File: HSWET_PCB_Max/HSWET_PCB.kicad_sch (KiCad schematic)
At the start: 21 parts, among them IC3 PS2565L-1-V-F3-A, IC4 PS2565L-1-V-F3-A, IC5 PS2565L-1-V-F3-A, J1 CON-SOCJ-2155, J2 emergency stop, J3 CON-SOCJ-2155, J4 turbine bus, U1 INA260AIPWR, U3 YAAJ_DCDC_StepDown_LM2596

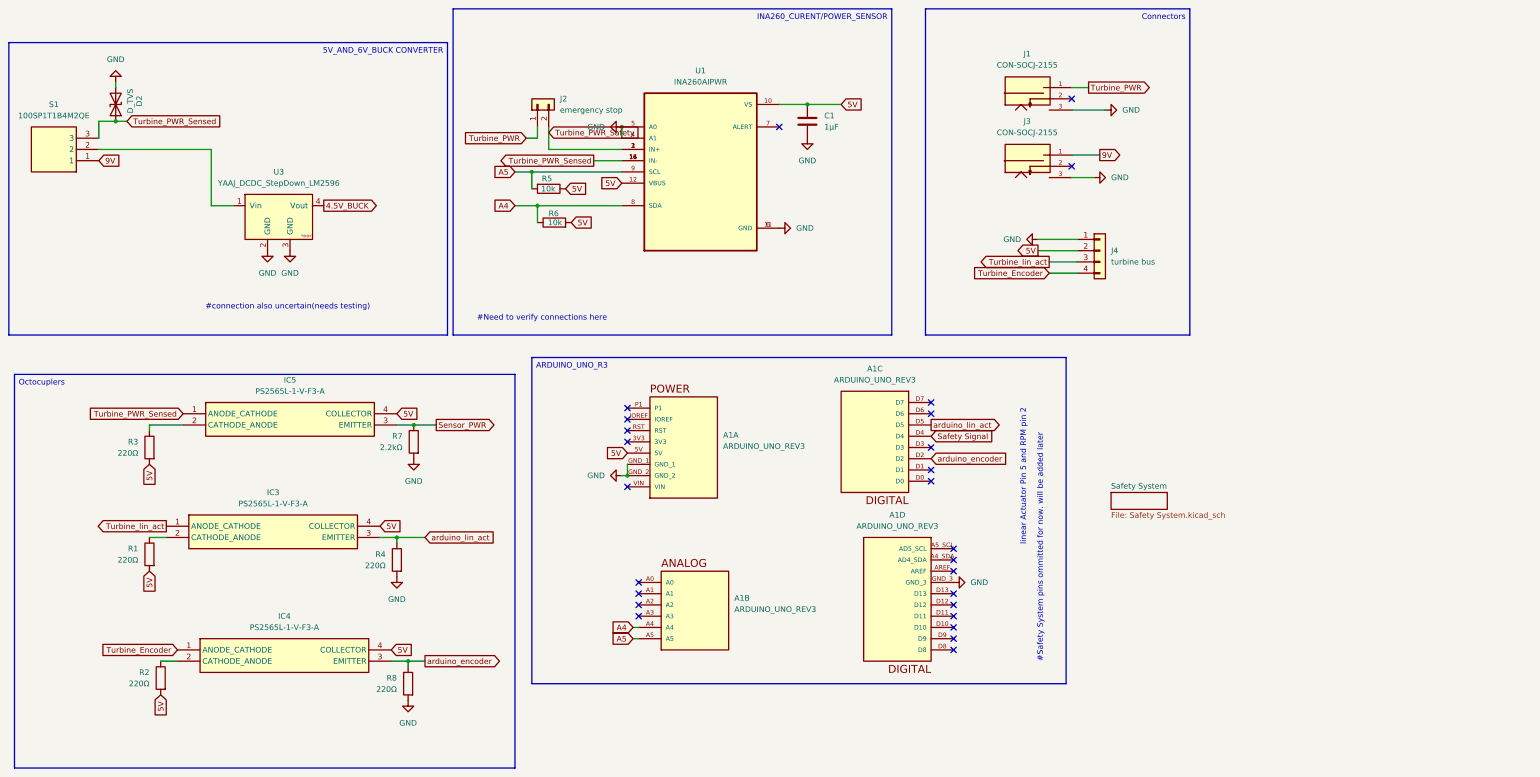
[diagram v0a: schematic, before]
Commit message: labelled everything, cleanup up various things, corrected inductor, removed schmitt
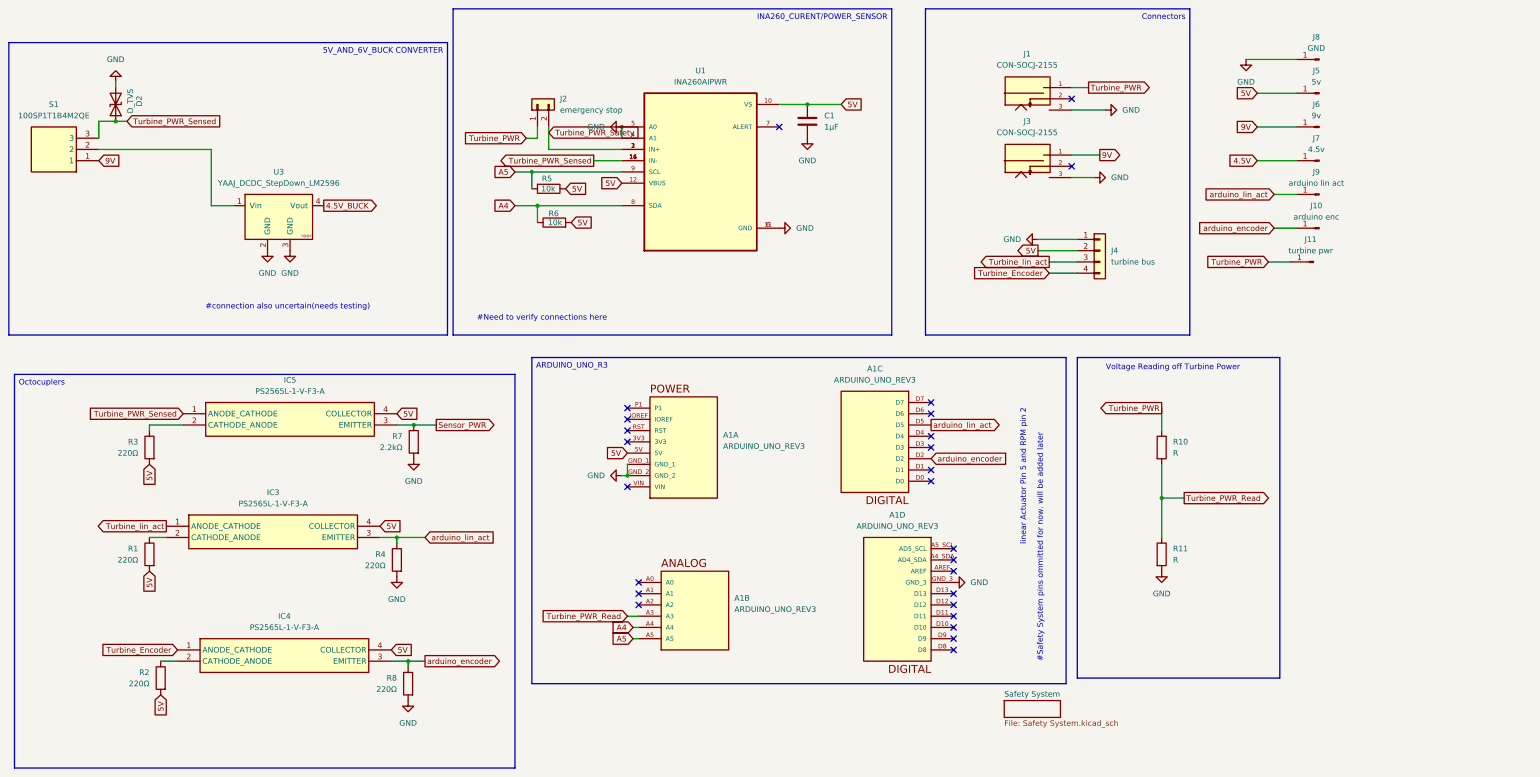
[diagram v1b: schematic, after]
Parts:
- added J10: arduino enc, Connector_PinHeader_1.00mm:PinHeader_1x01_P1.00mm_Vertical, symbol Connector:Conn_01x01_Pin
- added J11: turbine pwr, Connector_PinHeader_1.00mm:PinHeader_1x01_P1.00mm_Vertical, symbol Connector:Conn_01x01_Pin
- added J5: 5v, Connector_PinHeader_1.00mm:PinHeader_1x01_P1.00mm_Vertical, symbol Connector:Conn_01x01_Pin
- added J6: 9v, Connector_PinHeader_1.00mm:PinHeader_1x01_P1.00mm_Vertical, symbol Connector:Conn_01x01_Pin
- added J7: 4.5v, Connector_PinHeader_1.00mm:PinHeader_1x01_P1.00mm_Vertical, symbol Connector:Conn_01x01_Pin
- added J8: GND, Connector_PinHeader_1.00mm:PinHeader_1x01_P1.00mm_Vertical, symbol Connector:Conn_01x01_Pin
- added J9: arduino lin act, Connector_PinHeader_1.00mm:PinHeader_1x01_P1.00mm_Vertical, symbol Connector:Conn_01x01_Pin
- added R10, R11: R, Resistor_THT:R_Axial_DIN0207_L6.3mm_D2.5mm_P10.16mm_Horizontal, symbol Device:R
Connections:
- net 5V: now also J5.1 (Pin_1)
- net 9V: now also J6.1 (Pin_1)
- net GND: now also J8.1 (Pin_1), R11.2
- net Turbine_PWR: now also J11.1 (Pin_1), R10.1
- net arduino_encoder: now also J10.1 (Pin_1)
- net arduino_lin_act: now also J9.1 (Pin_1)
- net Turbine_PWR_Read: now reaches A1.A3
- net Turbine_PWR_Read: now also R10.2, R11.1
- net Safety Signal: no longer names the net of A1.D4
- new net 4.5V: J7.1 (Pin_1)
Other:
- note added: "Voltage Reading off Turbine Power"

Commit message: bruh
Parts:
- removed J1: CON-SOCJ-2155, footprints:GRAVITECH_CON-SOCJ-2155, symbol CON-SOCJ-2155:CON-SOCJ-2155
- added J1: TURBINE_IN, Connector_AMASS:AMASS_XT30PW-M_1x02_P2.50mm_Horizontal, symbol Connector_Generic:Conn_01x02
- added J12: LOAD_OUT, Connector_AMASS:AMASS_XT30PW-M_1x02_P2.50mm_Horizontal, symbol Connector_Generic:Conn_01x02
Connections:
- net GND: now also J1.2 (Pin_2), J12.2 (Pin_2)
- net Sensor_PWR: now also A1.A2
- net Turbine_PWR: now also J1.1 (Pin_1)
- net Turbine_PWR_Sensed: now also J12.1 (Pin_1)
- no-connect marks 26 -> 24

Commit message: made traces for power muuuuuuuuuuuuch bigger and added connector for load and removed 9v stuff just plug into the turbine
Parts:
- removed J3: CON-SOCJ-2155, footprints:GRAVITECH_CON-SOCJ-2155, symbol CON-SOCJ-2155:CON-SOCJ-2155
- removed J6: 9v, Connector_PinHeader_1.00mm:PinHeader_1x01_P1.00mm_Vertical, symbol Connector:Conn_01x01_Pin
- removed S1: 100SP1T1B4M2QE, footprints:100SP1T1B4M2QE, symbol 100SP1T1B4M2QE:100SP1T1B4M2QE
- J2: footprint Connector_PinHeader_2.54mm:PinHeader_1x02_P2.54mm_Vertical -> Connector_JST:JST_EH_B2B-EH-A_1x02_P2.50mm_Vertical
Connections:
- net 4.5V is gone; now on net 4.5V_BUCK: J7.1 (Pin_1)
- net Turbine_PWR_Sensed: now also U3.1 (Vin)
- no-connect marks 24 -> 23
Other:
- note added: "diode drains anything 40V+ to protect circuit :DDDDDDDDD"

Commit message: fixed lin act schematci
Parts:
- A1, IC3, IC4, IC5, J1, J12, J2, J4, U3: now not fitted
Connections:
- net 5V: no longer R1.2
- net GND: now also R1.2
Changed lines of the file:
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@@
 	(wire
 		(pts
-			(xy 137.16 40.64) (xy 137.16 45.72)
-		)
-		(stroke
-			(width 0)
-			(type default)
-		)
-	)
-	(wire
-		(pts
 			(xy 275.59 116.84) (xy 275.59 124.46)
 		)
@@
 	(wire
 		(pts
+			(xy 137.16 40.64) (xy 137.16 45.72)
+		)
+		(stroke
+			(width 0)
+			(type default)
+		)
+	)
+	(wire
+		(pts
 			(xy 134.62 43.18) (xy 134.62 40.64)
 		)
@@
 	)
 	(global_label "5V"
-		(shape input)
-		(at 46.99 140.97 270)
-		(fields_autoplaced yes)
-		(effects
-			(font
-				(size 1.27 1.27)
-			)
-			(justify right)
-		)
-		(property "Intersheetrefs" "${INTERSHEET_REFS}"
-			(at 46.99 146.2533 90)
-			(effects
-				(font
-					(size 1.27 1.27)
-				)
-				(justify right)
-				(hide yes)
-			)
-		)
-	)
-	(global_label "5V"
 		(shape output)
 		(at 247.65 68.58 180)
@@
 		(in_bom yes)
 		(on_board yes)
-		(dnp no)
+		(dnp yes)
 		(fields_autoplaced yes)
 		(property "Reference" "J4"
@@
 	)
 	(symbol
+		(lib_id "power:GND")
+		(at 46.99 140.97 0)
+		(unit 1)
+		(exclude_from_sim no)
+		(in_bom yes)
+		(on_board yes)
+		(dnp no)
+		(fields_autoplaced yes)
+		(property "Reference" "#PWR015"
+			(at 46.99 147.32 0)
+			(effects
+				(font
+					(size 1.27 1.27)
+				)
+				(hide yes)
+			)
+		)
+		(property "Value" "GND"
+			(at 46.99 146.05 0)
+			(effects
+				(font
+					(size 1.27 1.27)
+				)
+			)
+		)
+		(property "Footprint" ""
+			(at 46.99 140.97 0)
+			(effects
+				(font
+					(size 1.27 1.27)
+				)
+				(hide yes)
+			)
+		)
+		(property "Datasheet" ""
+			(at 46.99 140.97 0)
+			(effects
+				(font
+					(size 1.27 1.27)
+				)
+				(hide yes)
+			)
+		)
+		(property "Description" "Power symbol creates a global label with name \"GND\" , ground"
+			(at 46.99 140.97 0)
+			(effects
+				(font
+					(size 1.27 1.27)
+				)
+				(hide yes)
+			)
+		)
+		(pin "1"
+		)
+		(instances
+			(project ""
+				(path "/82d46295-621f-4df3-b604-ae215ede48d5"
+					(reference "#PWR015")
+					(unit 1)
+				)
+			)
+		)
+	)
+	(symbol
 		(lib_id "Device:R")
 		(at 46.99 113.03 0)
@@
 		(in_bom yes)
 		(on_board yes)
-		(dnp no)
+		(dnp yes)
 		(fields_autoplaced yes)
 		(property "Reference" "IC3"
@@
 		(in_bom yes)
 		(on_board yes)
-		(dnp no)
+		(dnp yes)
 		(fields_autoplaced yes)
 		(property "Reference" "IC5"
@@
 		(in_bom yes)
 		(on_board yes)
-		(dnp no)
+		(dnp yes)
 		(fields_autoplaced yes)
 		(property "Reference" "A1"
@@
 		(in_bom yes)
 		(on_board yes)
-		(dnp no)
+		(dnp yes)
 		(fields_autoplaced yes)
 		(property "Reference" "J12"
@@
 		(in_bom yes)
 		(on_board yes)
-		(dnp no)
+		(dnp yes)
 		(fields_autoplaced yes)
 		(property "Reference" "IC4"
@@
 		(in_bom yes)
 		(on_board yes)
-		(dnp no)
+		(dnp yes)
 		(fields_autoplaced yes)
 		(property "Reference" "J1"
@@
 		(in_bom yes)
 		(on_board yes)
-		(dnp no)
+		(dnp yes)
 		(fields_autoplaced yes)
 		(property "Reference" "J2"
@@
 		(in_bom yes)
 		(on_board yes)
-		(dnp no)
+		(dnp yes)
 		(fields_autoplaced yes)
 		(property "Reference" "U3"
@@
 		(in_bom yes)
 		(on_board yes)
-		(dnp no)
+		(dnp yes)
 		(fields_autoplaced yes)
 		(property "Reference" "A1"
@@
 		(in_bom yes)
 		(on_board yes)
-		(dnp no)
+		(dnp yes)
 		(fields_autoplaced yes)
 		(property "Reference" "A1"
@@
 		(in_bom yes)
 		(on_board yes)
-		(dnp no)
+		(dnp yes)
 		(fields_autoplaced yes)
 		(property "Reference" "A1"
